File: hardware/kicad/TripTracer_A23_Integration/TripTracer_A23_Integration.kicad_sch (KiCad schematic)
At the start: 0 parts

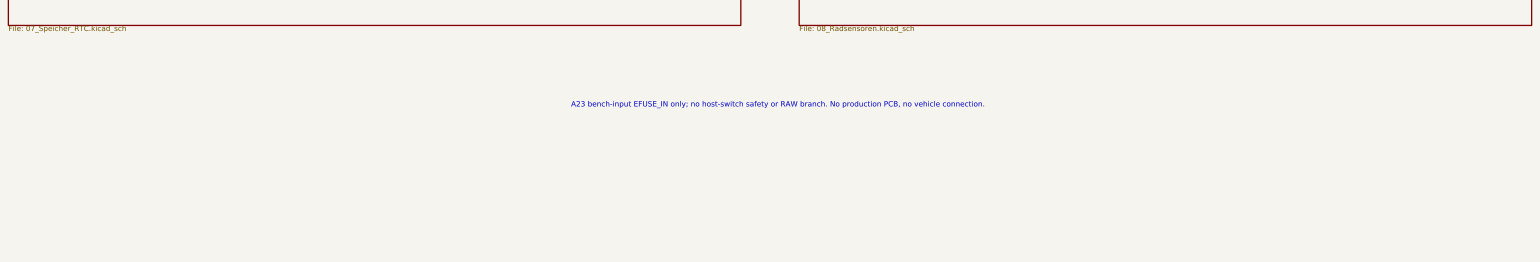
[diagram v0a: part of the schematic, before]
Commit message: TripPower A Round6 step4: real offboard M8 pins and fuses isolated from bench A23 input; host MCU HOLD 555 timer in same KiCad hierarchy; NO FAB
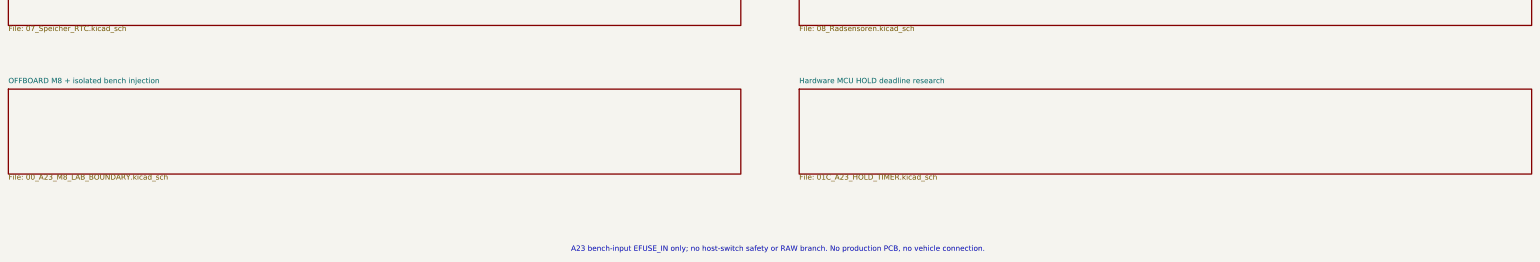
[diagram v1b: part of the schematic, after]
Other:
- added sheet Hardware MCU HOLD deadline research (01C_A23_HOLD_TIMER.kicad_sch)
- added sheet OFFBOARD M8 + isolated bench injection (00_A23_M8_LAB_BOUNDARY.kicad_sch)
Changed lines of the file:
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@@
  (property "Sheetfile" "08_Radsensoren.kicad_sch" (at 214.63 232.41 0) (effects (font (size 1.27 1.27)) (justify left top)))
  (instances (project "TripTracer_A23_Integration" (path "/a26d9b0c-7f10-4e5a-a65f-000000000064" (page "9")))))
- (text "A23 bench-input EFUSE_IN only; no host-switch safety or RAW branch. No production PCB, no vehicle connection." (at 209.55 251.46 0) (effects (font (size 1.27 1.27))))
- (sheet_instances (path "/" (page "1")))
+ (text "A23 bench-input EFUSE_IN only; no host-switch safety or RAW branch. No production PCB, no vehicle connection." (at 209.55 286.0 0) (effects (font (size 1.27 1.27))))
+ (sheet (at 25.4 247.65) (size 175.26 20.32) (exclude_from_sim no) (in_bom yes) (on_board yes) (dnp no)
+ (stroke (width 0) (type solid)) (fill (color 0 0 0 0))
+ (property "Sheetname" "OFFBOARD M8 + isolated bench injection" (at 25.4 246.38 0) (effects (font (size 1.27 1.27)) (justify left bottom)))
+ (property "Sheetfile" "00_A23_M8_LAB_BOUNDARY.kicad_sch" (at 25.4 267.97 0) (effects (font (size 1.27 1.27)) (justify left top)))
+ (instances (project "TripTracer_A23_Integration" (path "/a26d9b0c-7f10-4e5a-a65f-000000000064" (page "10"))))
+)
+(sheet (at 214.63 247.65) (size 175.26 20.32) (exclude_from_sim no) (in_bom yes) (on_board yes) (dnp no)
+ (stroke (width 0) (type solid)) (fill (color 0 0 0 0))
+ (property "Sheetname" "Hardware MCU HOLD deadline research" (at 214.63 246.38 0) (effects (font (size 1.27 1.27)) (justify left bottom)))
+ (property "Sheetfile" "01C_A23_HOLD_TIMER.kicad_sch" (at 214.63 267.97 0) (effects (font (size 1.27 1.27)) (justify left top)))
+ (instances (project "TripTracer_A23_Integration" (path "/a26d9b0c-7f10-4e5a-a65f-000000000064" (page "11"))))
+)
+(sheet_instances (path "/" (page "1")))
  (embedded_fonts no)
 )
